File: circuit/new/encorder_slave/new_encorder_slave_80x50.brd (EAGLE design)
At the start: 50 x 80 mm, 26 parts

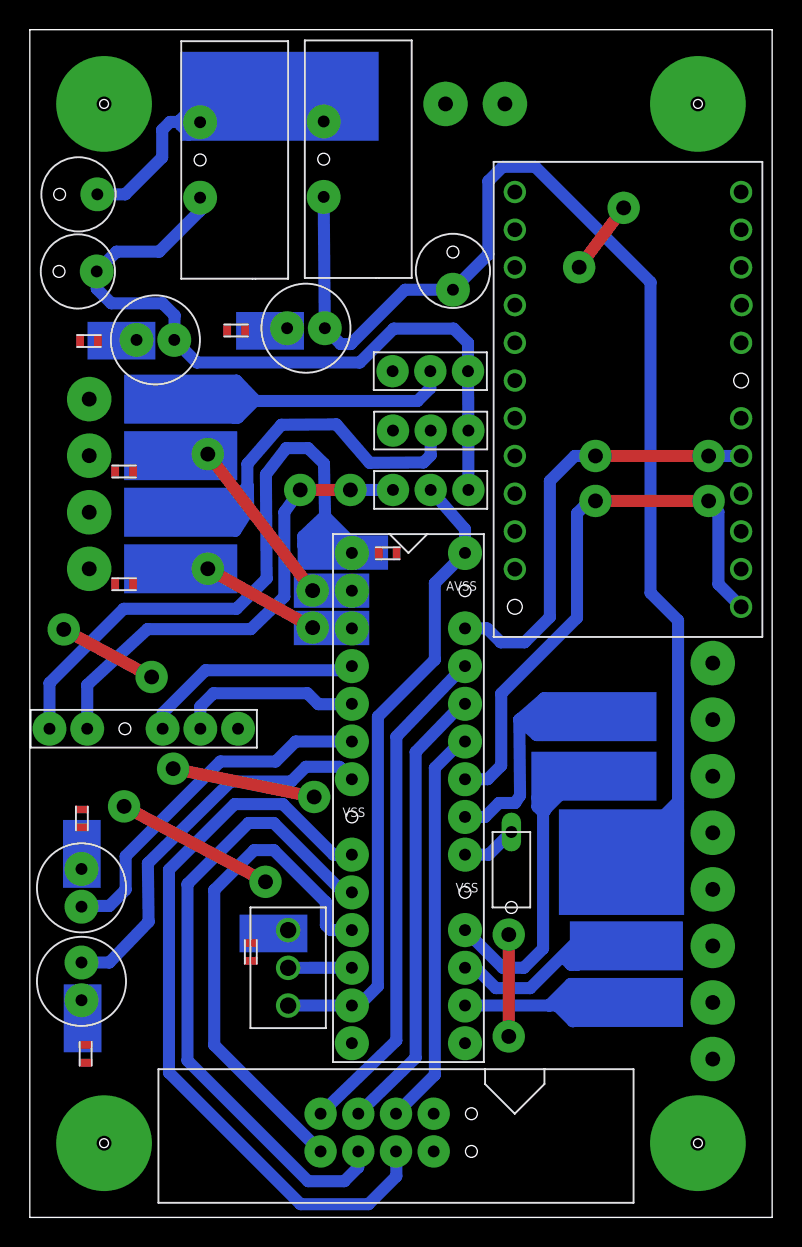
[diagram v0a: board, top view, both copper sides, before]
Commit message: 基板が間違っていたため上げなおし
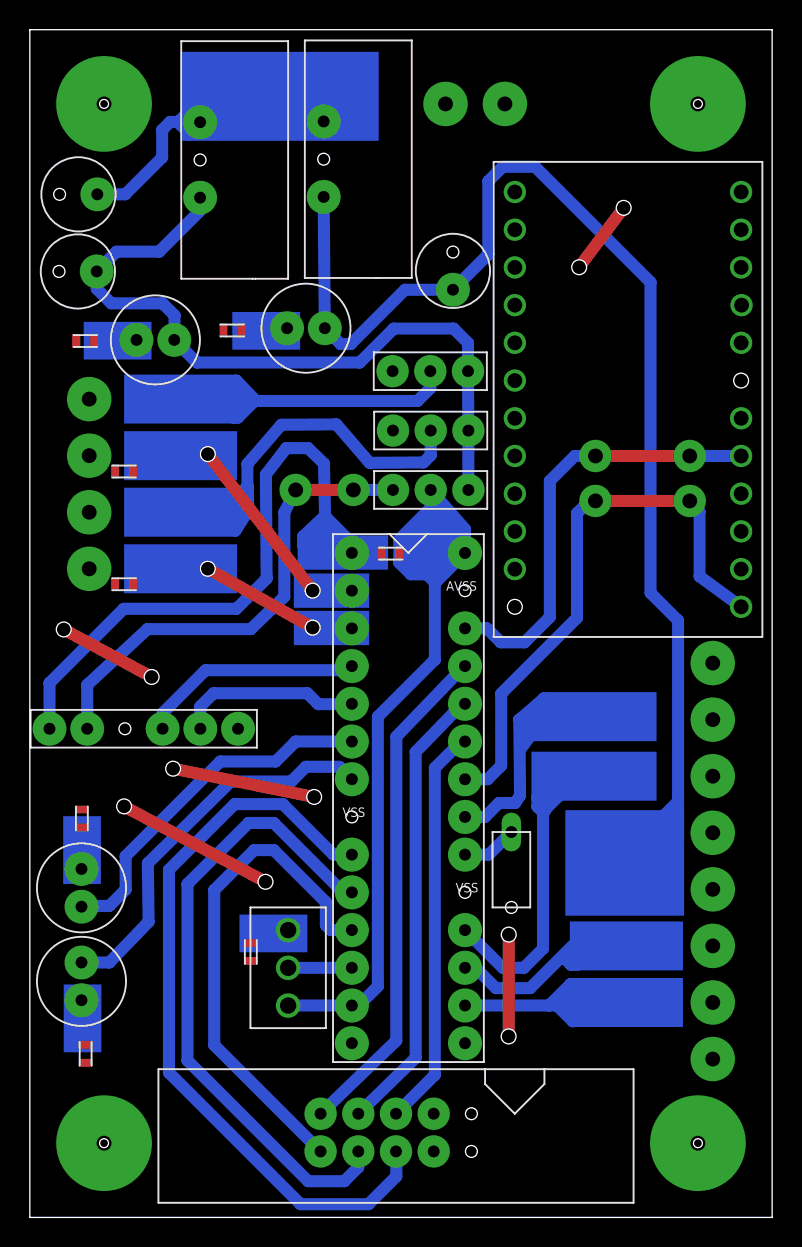
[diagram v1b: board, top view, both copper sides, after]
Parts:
- moved U$16 0.25 mm to (13.6, 59.7)
- moved U$18 0.25 mm to (3.73, 59.0)
- moved U$19 0.20 mm to (24.3, 44.7)
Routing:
- net S$25: track 43.3 -> 74.2 mm
- net S$35: track 0.00 -> 2.27 mm, vias 1 -> 0
- net S$66: track 7.62 -> 6.35 mm
- net S$65: track 7.62 -> 6.35 mm
- net S$36: track 2.19 -> 3.46 mm
- net S$64: track 8.02 -> 8.80 mm
- net S$60: track 3.38 -> 3.89 mm
